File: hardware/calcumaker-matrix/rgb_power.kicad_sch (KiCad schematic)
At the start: 11 parts, among them J2 VSYS IN (LED pwr), Q1 AO3401A, Q2 2N7002, U4 74LVC125

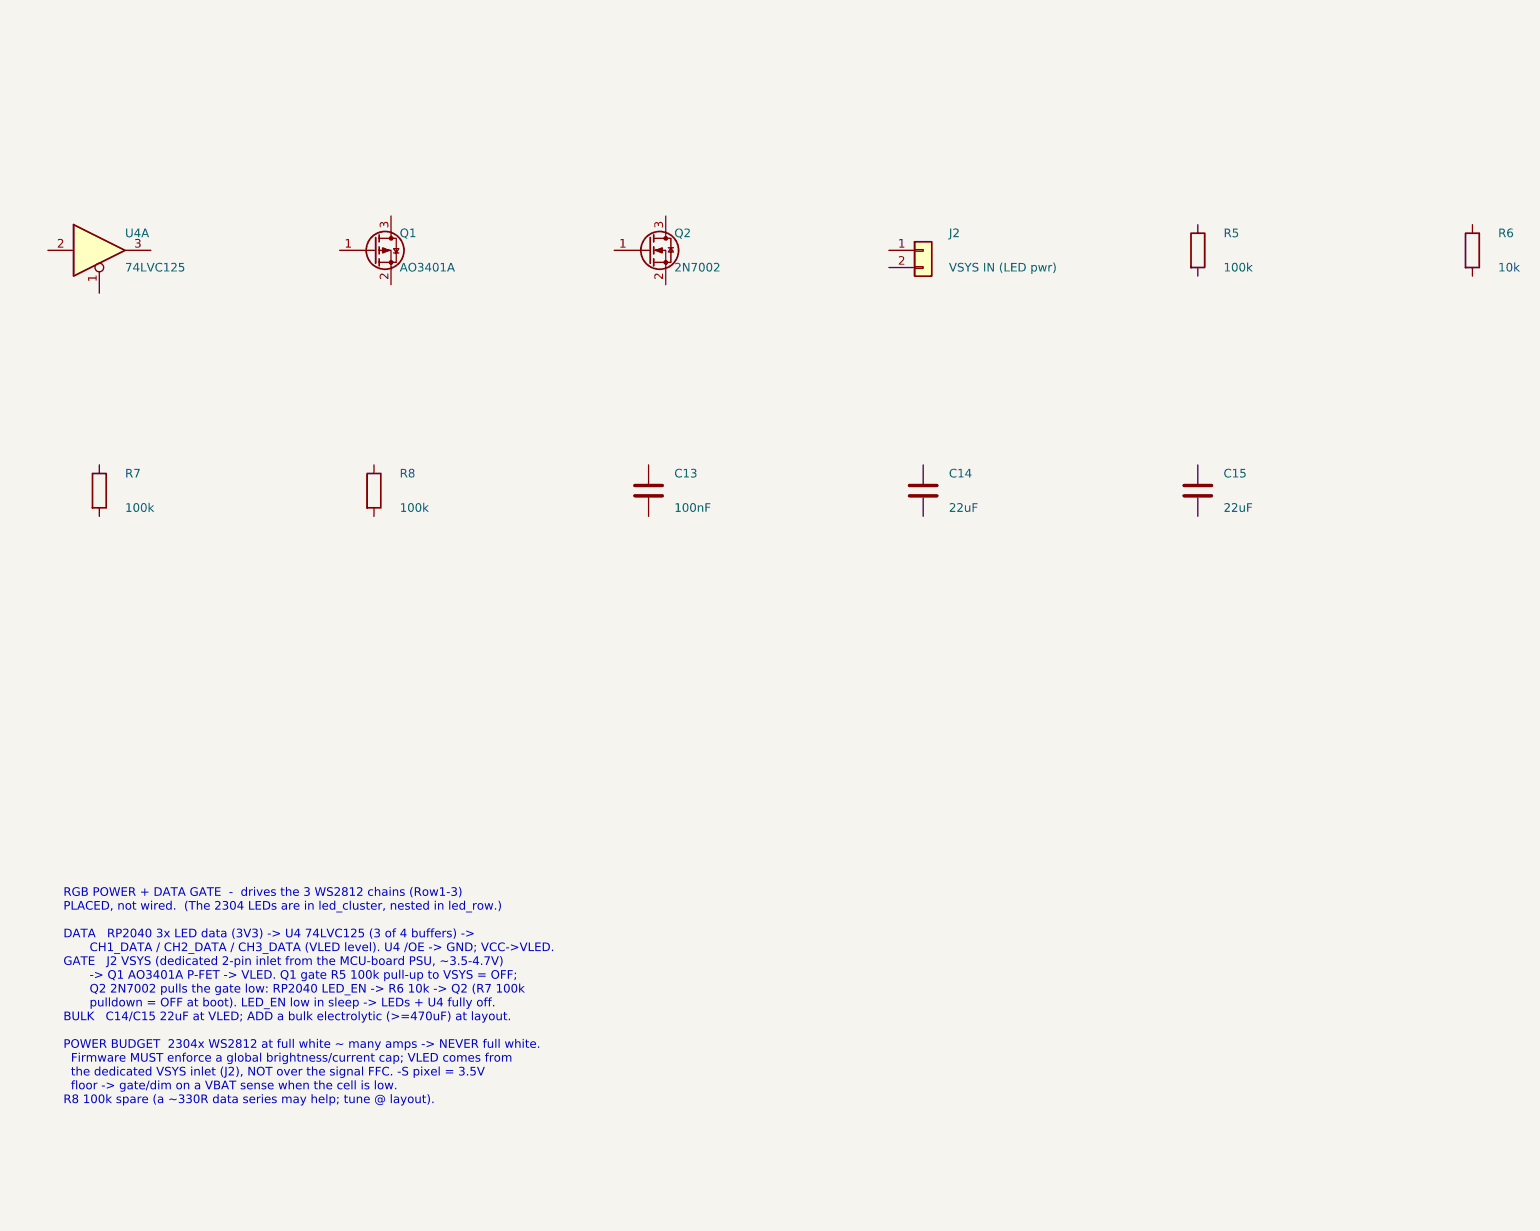
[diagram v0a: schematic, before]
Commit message: firmware: scaffold the two display-module targets + wire the module sheets
Firmware scaffold (all build; targets thumbv6m-none-eabi):
- calcumaker-display-proto: shared no_std wire protocol — the "display intent"
  DisplayFrame the U575 sends over SPI (text rows + flags + aux), with a
  fixed-length checksummed codec. Host-tested (cargo test: 3/3).
- calcumaker-display-fw: 7-seg module (STM32G031, embassy-stm32) — SPI-slave
  receiver + a bit-bang TM1640 driver + 7-seg render.
- calcumaker-matrix-fw: RGB-matrix module (RP2040, embassy-rp) — SPI-slave
  receiver + a 96x24 framebuffer/font blitter; WS2812 PIO output + SPI DMA
  stubbed as the bring-up TODOs.

Wire the one-off module schematic sheets (were placed-not-wired):
- kschgen: pin_geom now follows (extends ...) like pin_numbers, so derived
  symbols (STM32G031, 74xx) wire via net_pin.
- matrix rp2040 + rgb_power: RP2040 power/clock/flash/USB + the FET load switch
  and 3x single-gate level shifters are fully wired.
- display disp_mcu + disp_power: STM32G031 + the TPS61022 boost and 4x single-
  gate shifters are fully wired. (Quad 74xx buffers were multi-unit, which
  kschgen can't place fully, so the shifters are single-gate 74x1G125 — matching
  the keyboard's approach.)

All 4 boards check clean (mcu 46 / keyboard 179 / display 83 / matrix 2343, no
dup refs); wiring cut ERC pin_not_connected ~4x on both display modules.

Co-Authored-By: Claude Opus 4.8 (1M context) <noreply@anthropic.com>
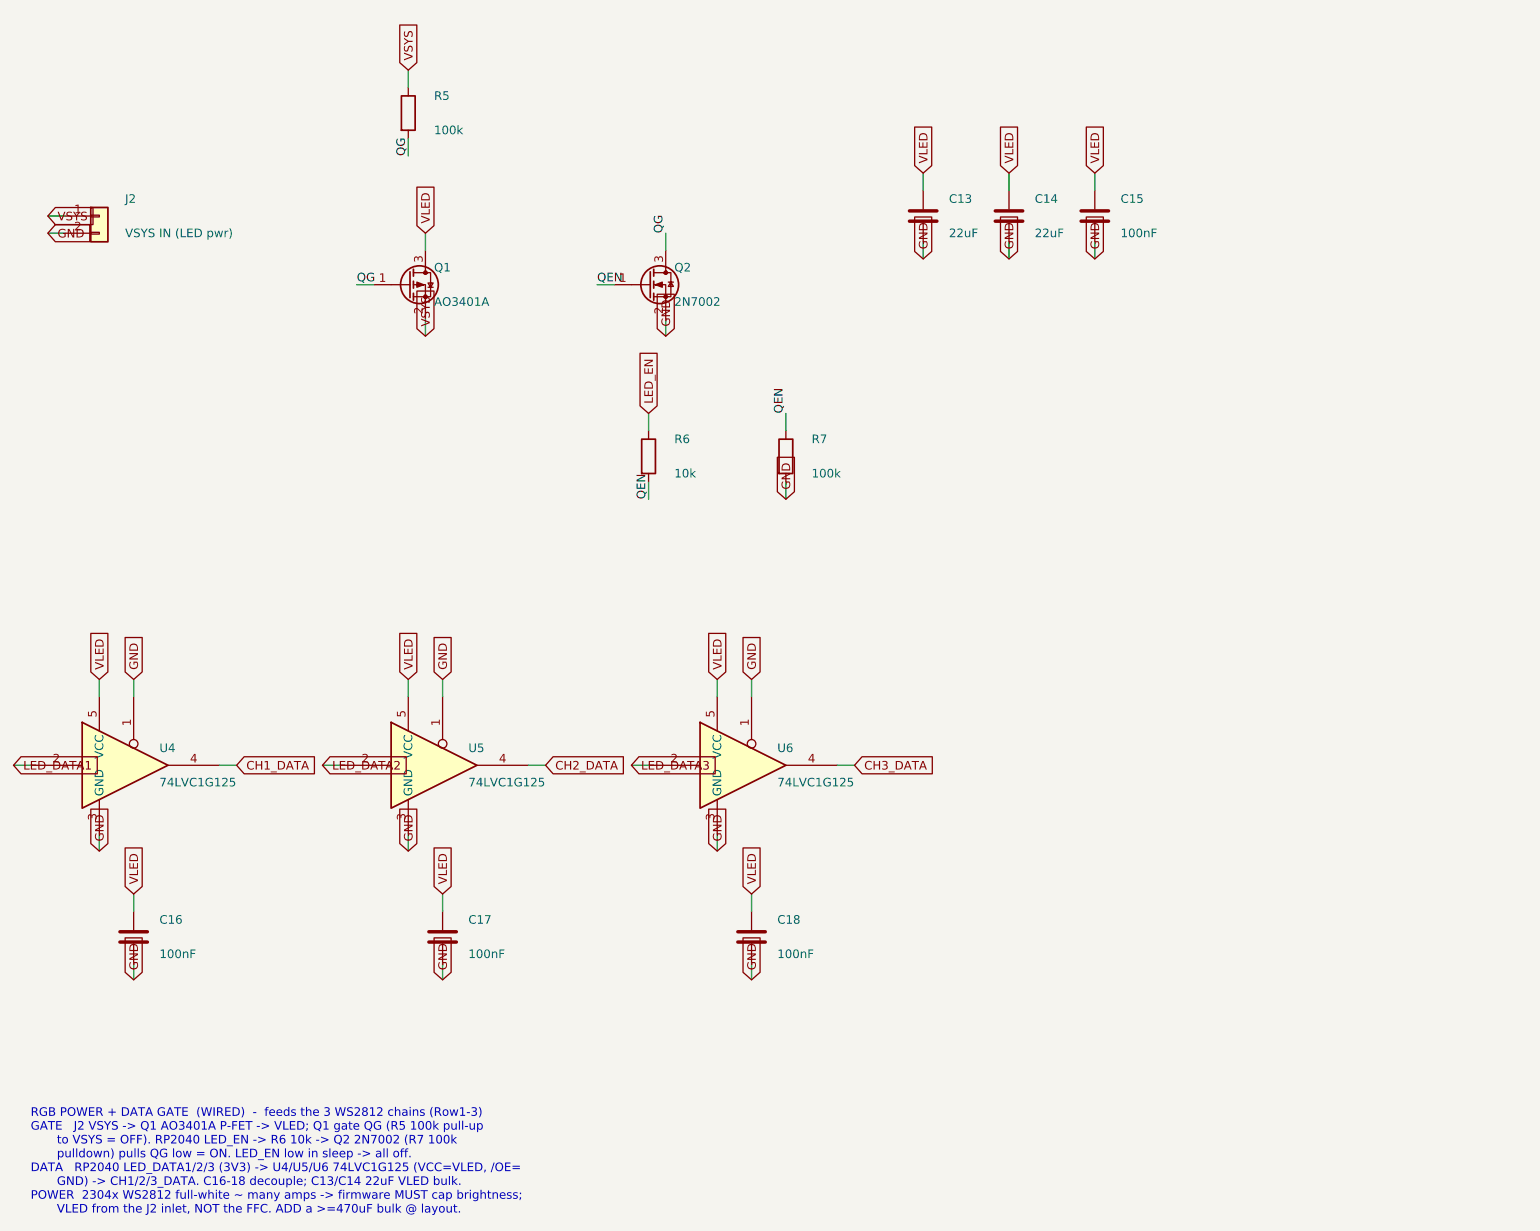
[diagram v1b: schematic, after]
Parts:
- removed R8: 100k, Resistor_SMD:R_0402_1005Metric, symbol Device:R
- removed U4: 74LVC125, Package_SO:SOIC-14_3.9x8.7mm_P1.27mm, symbol 74xx:74LVC125
- added C16, C17, C18: 100nF, Capacitor_SMD:C_0402_1005Metric, symbol Device:C
- added U4, U5, U6: 74LVC1G125, Package_TO_SOT_SMD:SOT-23-5, symbol 74xGxx:74LVC1G125
- C13: value 100nF -> 22uF; footprint Capacitor_SMD:C_0402_1005Metric -> Capacitor_SMD:C_0603_1608Metric; LCSC C1525 -> C45783
- C15: value 22uF -> 100nF; footprint Capacitor_SMD:C_0603_1608Metric -> Capacitor_SMD:C_0402_1005Metric; LCSC C45783 -> C1525
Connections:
- net LED_EN: now reaches R6.1
- net QEN: now reaches R6.2
- net QEN: now also Q2.1 (G), R7.1
- net VLED: now reaches C15.1
- net VLED: now also C13.1, C14.1, Q1.3 (D), C16.1, C17.1, C18.1, U4.5 (VCC), U5.5 (VCC), U6.5 (VCC)
- net GND: now reaches C15.2
- net GND: now also C13.2, C14.2, J2.2 (Pin_2), Q2.2 (S), R7.2, C16.2, C17.2, C18.2, U4.1, U4.3 (GND), U5.1, U5.3 (GND), U6.1, U6.3 (GND)
- net VSYS: now reaches J2.1 (Pin_1)
- net VSYS: now also Q1.2 (S), R5.1
- net QG: now reaches Q2.3 (D)
- net QG: now also Q1.1 (G), R5.2
- new net CH1_DATA: U4.4
- new net CH2_DATA: U5.4
- new net CH3_DATA: U6.4
- new net LED_DATA1: U4.2
- new net LED_DATA2: U5.2
- new net LED_DATA3: U6.2
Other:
- note added: "RGB POWER + DATA GATE (WIRED) - feeds the 3 WS2812 chains (Row1-3) GATE J2 VSYS -> Q1 AO3401A P-FET -> VLED; Q1 gate QG (R5 100k pull-up to VSYS = OFF). RP2040 LED_EN -> R6 10k -> Q2 2N7002 (R7 100k pulldown) pulls QG low = ON. LED_EN low in sleep -> all off. DATA RP2040 LED_DATA1/2/3 (3V3) -> U4/U5/U6 74LVC1G125 (VCC=VLED, /OE= GND) -> CH1/2/3_DATA. C16-18 decouple; C13/C14 22uF VLED bulk. POWER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"
- note removed: "RGB POWER + DATA GATE - drives the 3 WS2812 chains (Row1-3) PLACED, not wired. (The 2304 LEDs are in led_cluster, nested in led_row.) DATA RP2040 3x LED data (3V3) -> U4 74LVC125 (3 of 4 buffers) -> CH1_DATA / CH2_DATA / CH3_DATA (VLED level). U4 /OE -> GND; VCC->VLED. GATE J2 VSYS (dedicated 2-pin inlet from the MCU-board PSU, ~3.5-4.7V) -> Q1 AO3401A P-FET -> VLED. Q1 gate R5 100k pull-up to VS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"
- title: Calcumaker 16 — RGB Matrix — RGB power + data gate (quad level shift + VLED load switch) -> Calcumaker 16 — RGB Matrix — RGB power + data gate (load switch + 3x level shift)
